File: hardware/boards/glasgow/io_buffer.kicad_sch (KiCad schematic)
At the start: 68 parts, among them J2 IDC-Header_2x10_P2.54mm, J8 Conn_01x08, J9 Conn_01x08, U10 SN74LVC1T45DCKR, U11 SN74LVC1T45DCKR, U16 SN74LVC1T45DCKR, U17 SN74LVC1T45DCKR, U18 SN74LVC1T45DCKR, U19 PCA6408APW, U20 DAC081C081CIMK, U21 INA233, U31 TPS73101DBV, U4 SN74LVC1T45DCKR, U6 SN74LVC1T45DCKR, U9 SN74LVC1T45DCKR

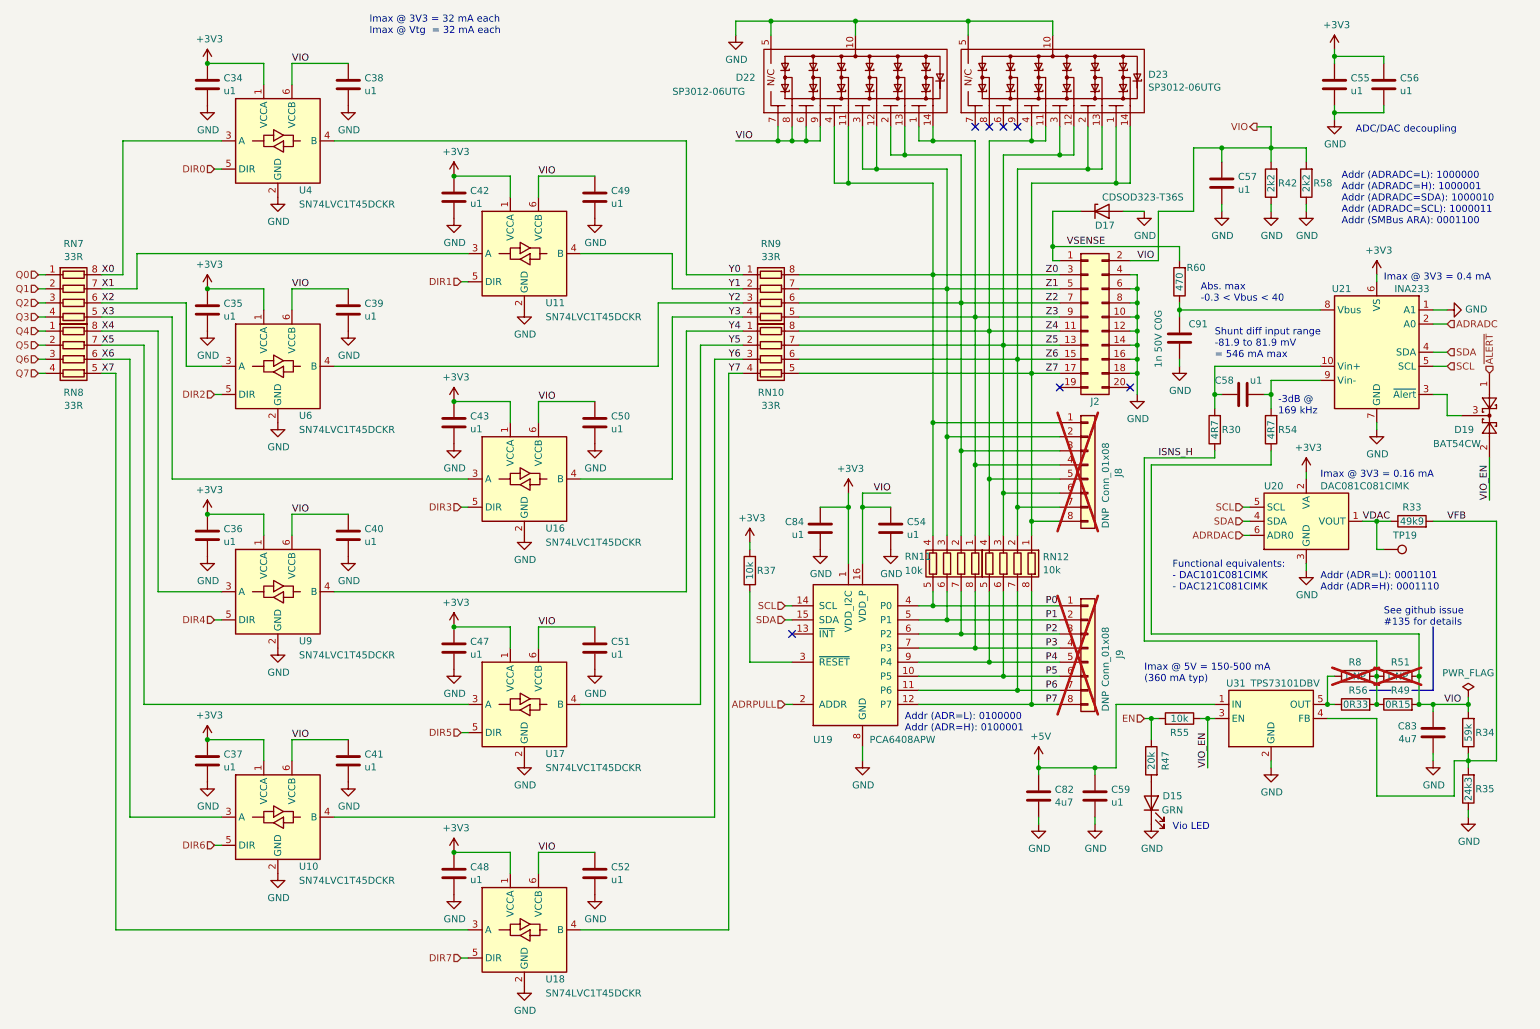
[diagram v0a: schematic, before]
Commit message: Remove one of the sides
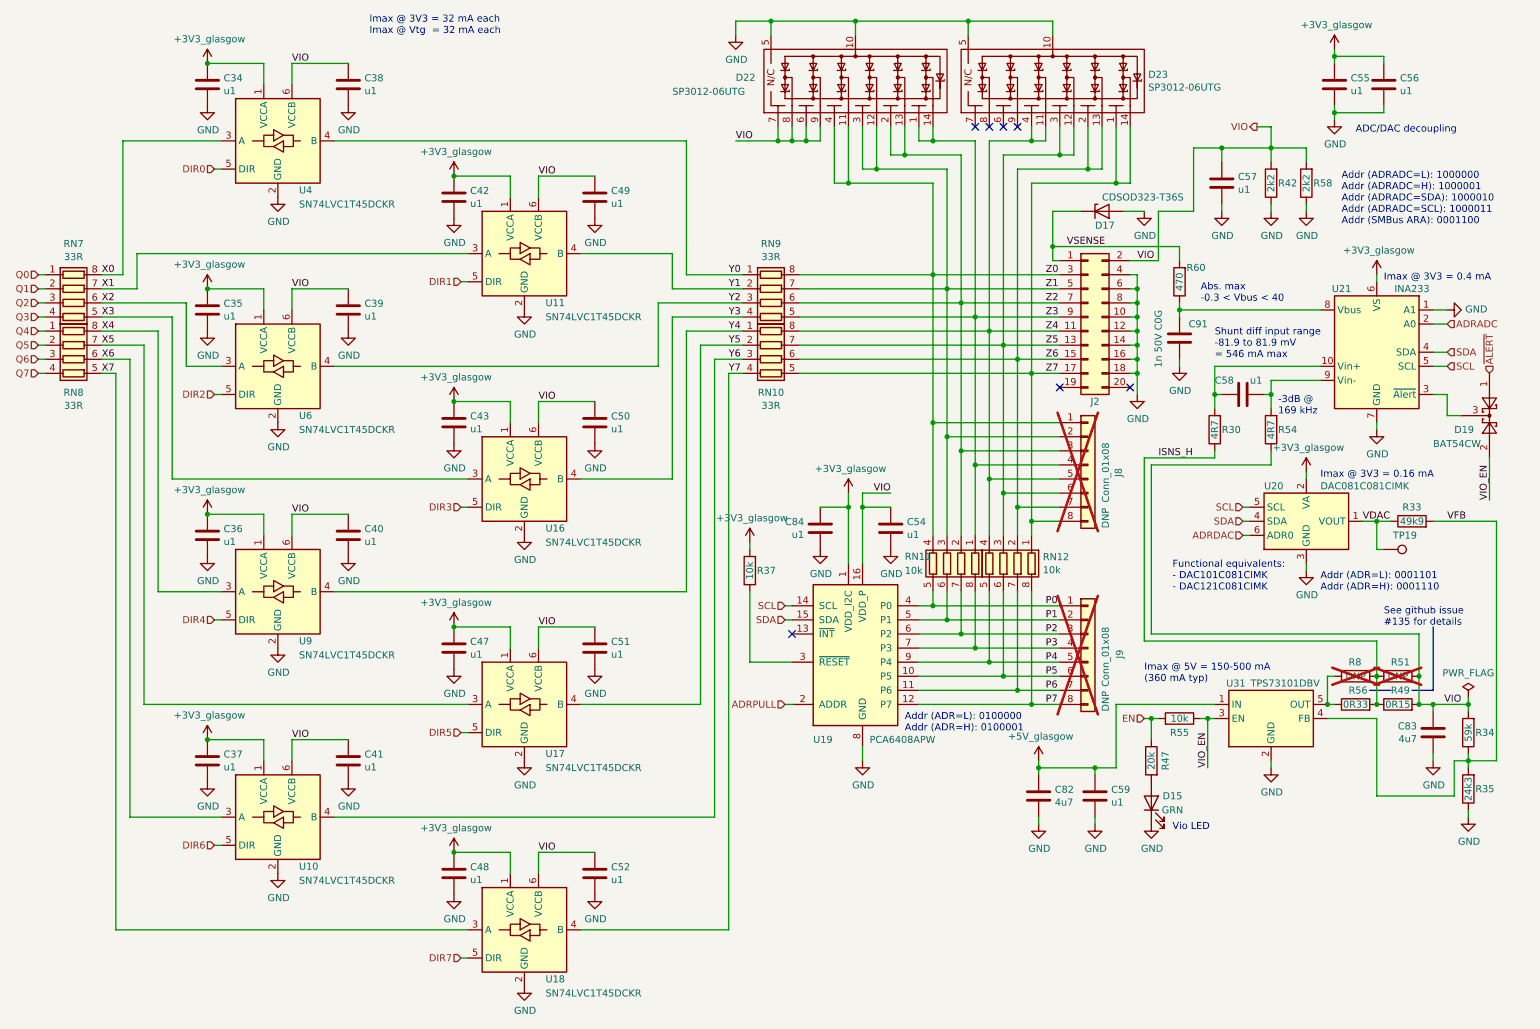
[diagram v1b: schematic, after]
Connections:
- net +3V3 renamed +3V3_glasgow
- net +5V renamed +5V_glasgow
